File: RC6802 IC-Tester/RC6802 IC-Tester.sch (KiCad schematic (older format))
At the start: 66 parts, among them J2 RC6802_UI_Port, M1 Mounting, M2 Mounting, M3 Mounting, M4 Mounting, Q1 2N3906, Q2 2N3906, Q3 2N3906, Q4 2N3904, Q5 2N3906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

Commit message: IC-Tester layout
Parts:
- D1, D2: footprint (none) -> LEDs:LED_D5.0mm
- D3: value STBY -> SBY; footprint (none) -> LEDs:LED_D5.0mm
- D4: value OK -> PWR; footprint (none) -> LEDs:LED_D5.0mm
- D5, D6: footprint (none) -> Diodes_THT:D_DO-35_SOD27_P7.62mm_Horizontal
- U3: footprint (none) -> ZIF:ZIF-16
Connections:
- net D3: no longer U2.8 (D3)
- net D4: no longer U2.13 (D4)
- net D5: no longer U2.14 (D5)
- net D6: no longer U2.17 (D6)
- net D7: no longer U2.18 (D7)
- net GND: now also U2.13 (D4), U2.14 (D5), U2.17 (D6), U2.18 (D7), U2.8 (D3)
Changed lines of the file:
@@
 Text Label 1625 6100 0    60   ~ 0
 D2
-Text Label 1625 6200 0    60   ~ 0
-D3
-Text Label 1625 6300 0    60   ~ 0
-D4
-Text Label 1625 6400 0    60   ~ 0
-D5
-Text Label 1625 6500 0    60   ~ 0
-D6
-Text Label 1625 6600 0    60   ~ 0
-D7
-Entry Wire Line
-	1600 6200 1500 6300
-Entry Wire Line
-	1600 6300 1500 6400
-Entry Wire Line
-	1600 6400 1500 6500
-Entry Wire Line
-	1600 6500 1500 6600
-Entry Wire Line
-	1600 6600 1500 6700
 Entry Wire Line
 	1600 6000 1500 6100
@@
 F 0 "U3" H 10475 3625 50  0000 C CNN
 F 1 "ZIF-16" H 10475 3125 50  0000 C CNN
-F 2 "" H 10475 3625 50  0001 C CNN
+F 2 "ZIF:ZIF-16" H 10475 3625 50  0001 C CNN
 F 3 "" H 10475 3625 50  0001 C CNN
 	1    10475 3625
@@
 F 0 "D2" H 13050 3875 50  0000 L CNN
 F 1 "16" H 12850 3775 50  0000 L CNN
-F 2 "" V 13000 3825 50  0001 C CNN
+F 2 "LEDs:LED_D5.0mm" V 13000 3825 50  0001 C CNN
 F 3 "" V 13000 3825 50  0001 C CNN
 	1    13000 3825
@@
 F 0 "D1" H 12850 3875 50  0000 L CNN
 F 1 "14" H 12650 3775 50  0000 L CNN
-F 2 "" V 12800 3825 50  0001 C CNN
+F 2 "LEDs:LED_D5.0mm" V 12800 3825 50  0001 C CNN
 F 3 "" V 12800 3825 50  0001 C CNN
 	1    12800 3825
@@
 	1875 6100 1600 6100
 Wire Wire Line
-	1875 6200 1600 6200
-Wire Wire Line
-	1875 6300 1600 6300
-Wire Wire Line
-	1875 6600 1600 6600
-Wire Wire Line
-	1875 6500 1600 6500
-Wire Wire Line
-	1875 6400 1600 6400
-Wire Wire Line
 	1600 6800 1875 6800
 Wire Bus Line
@@
 P 13825 3825
 F 0 "D4" H 13875 3875 50  0000 L CNN
-F 1 "OK" H 13650 3750 50  0000 L CNN
-F 2 "" V 13825 3825 50  0001 C CNN
+F 1 "PWR" H 13625 3750 50  0000 L CNN
+F 2 "LEDs:LED_D5.0mm" V 13825 3825 50  0001 C CNN
 F 3 "" V 13825 3825 50  0001 C CNN
 	1    13825 3825
@@
 P 13625 3825
 F 0 "D3" H 13675 3875 50  0000 L CNN
-F 1 "STBY" H 13425 3750 50  0000 L CNN
-F 2 "" V 13625 3825 50  0001 C CNN
+F 1 "SBY" H 13425 3750 50  0000 L CNN
+F 2 "LEDs:LED_D5.0mm" V 13625 3825 50  0001 C CNN
 F 3 "" V 13625 3825 50  0001 C CNN
 	1    13625 3825
@@
 F 0 "D5" H 6850 4005 50  0000 L CNN
 F 1 "1N4148" H 6750 3845 50  0000 L CNN
-F 2 "" V 6900 3925 50  0001 C CNN
+F 2 "Diodes_THT:D_DO-35_SOD27_P7.62mm_Horizontal" V 6900 3925 50  0001 C CNN
 F 3 "" V 6900 3925 50  0001 C CNN
 	1    6900 3925
@@
 F 0 "D6" H 6850 4630 50  0000 L CNN
 F 1 "1N4148" H 6750 4470 50  0000 L CNN
-F 2 "" V 6900 4550 50  0001 C CNN
+F 2 "Diodes_THT:D_DO-35_SOD27_P7.62mm_Horizontal" V 6900 4550 50  0001 C CNN
 F 3 "" V 6900 4550 50  0001 C CNN
 	1    6900 4550
@@
 Wire Bus Line
 	10475 1900 3300 1900
+$Comp
+L GND #PWR?
+U 1 1 5E0237F4
+P 1650 6300
+F 0 "#PWR?" H 1650 6050 50  0001 C CNN
+F 1 "GND" H 1650 6150 50  0000 C CNN
+F 2 "" H 1650 6300 50  0001 C CNN
+F 3 "" H 1650 6300 50  0001 C CNN
+	1    1650 6300
+	1    0    0    -1
+$EndComp
+Wire Wire Line
+	1650 6300 1650 6200
+Wire Wire Line
+	1650 6200 1875 6200
+Wire Wire Line
+	1875 6300 1775 6300
+Wire Wire Line
+	1775 6200 1775 6600
+Connection ~ 1775 6200
+Wire Wire Line
+	1775 6400 1875 6400
+Connection ~ 1775 6300
+Wire Wire Line
+	1775 6500 1875 6500
+Connection ~ 1775 6400
+Wire Wire Line
+	1775 6600 1875 6600
+Connection ~ 1775 6500
 $EndSCHEMATC

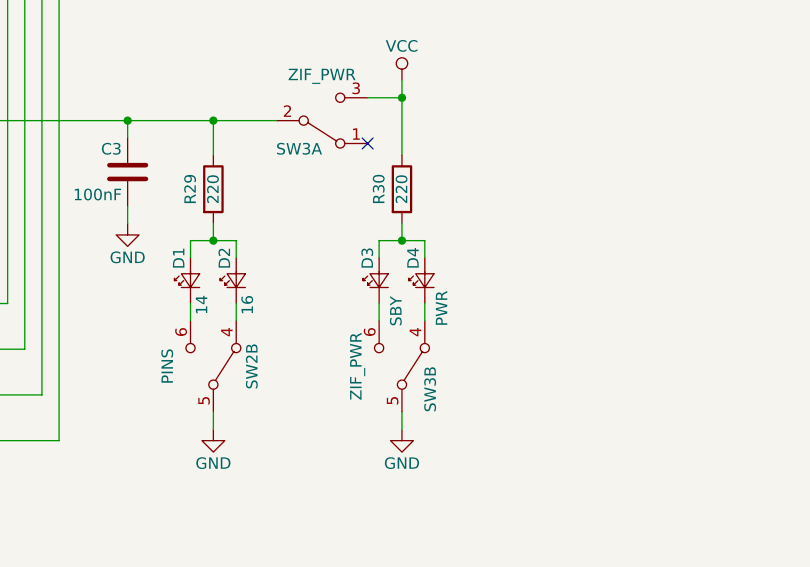
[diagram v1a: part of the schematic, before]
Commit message: PWR/SBY LEDs swapped
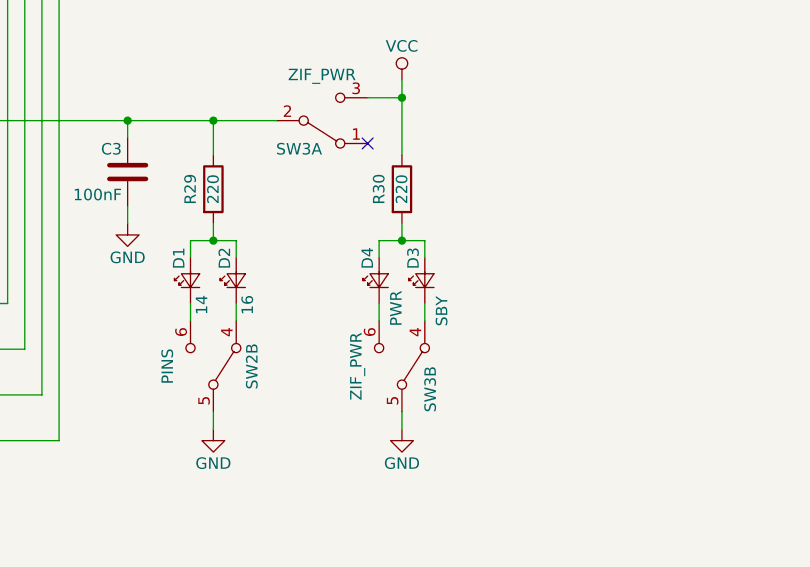
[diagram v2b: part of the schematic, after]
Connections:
- net at SW3.4 (A): now also D3.1 (K); no longer D4.1 (K)
- net at SW3.6 (C): now also D4.1 (K); no longer D3.1 (K)
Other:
- moved on the sheet: D3, D4
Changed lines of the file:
@@
 L LED_Small D4
 U 1 1 5E0023D0
+P 13625 3825
+F 0 "D4" H 13675 3875 50  0000 L CNN
+F 1 "PWR" H 13425 3750 50  0000 L CNN
+F 2 "LEDs:LED_D5.0mm" V 13625 3825 50  0001 C CNN
+F 3 "" V 13625 3825 50  0001 C CNN
+	1    13625 3825
+	0    -1   -1   0
+$EndComp
+$Comp
+L LED_Small D3
+U 1 1 5E0023D6
 P 13825 3825
-F 0 "D4" H 13875 3875 50  0000 L CNN
-F 1 "PWR" H 13625 3750 50  0000 L CNN
+F 0 "D3" H 13875 3875 50  0000 L CNN
+F 1 "SBY" H 13625 3750 50  0000 L CNN
 F 2 "LEDs:LED_D5.0mm" V 13825 3825 50  0001 C CNN
 F 3 "" V 13825 3825 50  0001 C CNN
@@
 	0    -1   -1   0
 $EndComp
-$Comp
-L LED_Small D3
-U 1 1 5E0023D6
-P 13625 3825
-F 0 "D3" H 13675 3875 50  0000 L CNN
-F 1 "SBY" H 13425 3750 50  0000 L CNN
-F 2 "LEDs:LED_D5.0mm" V 13625 3825 50  0001 C CNN
-F 3 "" V 13625 3825 50  0001 C CNN
-	1    13625 3825
-	0    -1   -1   0
-$EndComp

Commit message: IC-Tester original code
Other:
- note added: "$2000"
- note added: "$2400"
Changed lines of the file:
@@
 	1775 6600 1875 6600
 Connection ~ 1775 6500
+Text Notes 2450 11025 0    60   ~ 0
+$2000
+Text Notes 2450 7050 0    60   ~ 0
+$2400
 $EndSCHEMATC
